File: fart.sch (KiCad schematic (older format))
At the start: 2 parts

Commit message: Add files via upload
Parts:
- U1: renamed from U?; footprint (none) -> Housings_DIP:DIP-40_W15.24mm_Socket_LongPads
- X1: renamed from X?; footprint (none) -> fart:Cart_Conn
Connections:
- net ROMC3: now reaches X1.10 (ROMC3)
- net ROMC3: now also U1.38 (ROMC3)
- net D3: now reaches X1.11 (D3)
- net D3: now also U1.19 (D3)
- net ROMC4: now reaches X1.12 (ROMC4)
- net ROMC4: now also U1.39 (ROMC4)
- net PHI: now reaches X1.13 (PHI)
- net PHI: now also U1.2 (PHI)
- net D4: now reaches X1.14 (D4)
- net D4: now also U1.21 (D4)
- net WRITE: now reaches X1.15 (WRITE)
- net WRITE: now also U1.3 (WRITE)
- net D5: now reaches X1.16 (D5)
- net D5: now also U1.22 (D5)
- net D6: now reaches X1.17 (D6)
- net D6: now also U1.23 (D6)
- net D7: now reaches X1.18 (D7)
- net D7: now also U1.24 (D7)
- net D0: now reaches X1.3 (D0)
- net D0: now also U1.16 (D0)
- net D1: now reaches X1.4 (D1)
- net D1: now also U1.17 (D1)
- net ~INTREQ: now reaches X1.5 (~INTREQ)
- net ~INTREQ: now also U1.4 (~INT_REQ)
- net ROMC0: now reaches X1.6 (ROMC0)
- net ROMC0: now also U1.35 (ROMC0)
- net ROMC1: now reaches X1.7 (ROMC1)
- net ROMC1: now also U1.36 (ROMC1)
- net ROMC2: now reaches X1.8 (ROMC2)
- net ROMC2: now also U1.37 (ROMC2)
- net D2: now reaches X1.9 (D2)
- net D2: now also U1.18 (D2)
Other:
- note added: "Vdd current: 70mA max"
- note added: "Vgg current: 70mA max"
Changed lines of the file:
@@
 $EndDescr
 $Comp
-L fart:CartConn X?
+L fart:CartConn X1
 U 1 1 5D1E5303
 P 7000 3100
-F 0 "X?" H 7228 3146 50  0000 L CNN
+F 0 "X1" H 7228 3146 50  0000 L CNN
 F 1 "CartConn" H 7228 3055 50  0000 L CNN
-F 2 "" H 6950 3100 50  0001 C CNN
+F 2 "fart:Cart_Conn" H 7000 1850 50  0000 C CNN
 F 3 "" H 6950 3100 50  0001 C CNN
 	1    7000 3100
@@
 $EndComp
 $Comp
-L fart:F3853 U?
+L fart:F3853 U1
 U 1 1 5D1E6D1B
 P 4000 3000
-F 0 "U?" H 4000 4175 50  0000 C CNN
+F 0 "U1" H 4000 4175 50  0000 C CNN
 F 1 "F3853" H 4000 4084 50  0000 C CNN
-F 2 "" H 4000 3000 50  0001 C CNN
+F 2 "Housings_DIP:DIP-40_W15.24mm_Socket_LongPads" H 4000 1900 50  0000 C CNN
 F 3 "" H 4000 3000 50  0001 C CNN
 	1    4000 3000
@@
 $EndComp
 $Comp
-L power:GND #PWR?
+L power:GND #PWR0101
 U 1 1 5D1E8B6D
 P 6400 2000
-F 0 "#PWR?" H 6400 1750 50  0001 C CNN
+F 0 "#PWR0101" H 6400 1750 50  0001 C CNN
 F 1 "GND" V 6405 1872 50  0001 R CNN
 F 2 "" H 6400 2000 50  0001 C CNN
@@
 	6500 2000 6400 2000
 $Comp
-L power:GND #PWR?
+L power:GND #PWR0102
 U 1 1 5D1E9405
 P 3400 3950
-F 0 "#PWR?" H 3400 3700 50  0001 C CNN
+F 0 "#PWR0102" H 3400 3700 50  0001 C CNN
 F 1 "GND" V 3405 3822 50  0001 R CNN
 F 2 "" H 3400 3950 50  0001 C CNN
@@
 $EndComp
 $Comp
-L power:+5V #PWR?
+L power:+5V #PWR0103
 U 1 1 5D1EA69B
 P 6450 3900
-F 0 "#PWR?" H 6450 3750 50  0001 C CNN
+F 0 "#PWR0103" H 6450 3750 50  0001 C CNN
 F 1 "+5V" V 6465 4028 50  0000 L CNN
 F 2 "" H 6450 3900 50  0001 C CNN
@@
 	6500 3900 6600 3900
 $Comp
-L power:+12V #PWR?
+L power:+12V #PWR0104
 U 1 1 5D1EBC41
 P 6600 4200
-F 0 "#PWR?" H 6600 4050 50  0001 C CNN
+F 0 "#PWR0104" H 6600 4050 50  0001 C CNN
 F 1 "+12V" V 6615 4328 50  0000 L CNN
 F 2 "" H 6600 4200 50  0001 C CNN
@@
 $EndComp
 $Comp
-L power:+5V #PWR?
+L power:+5V #PWR0105
 U 1 1 5D1EC708
 P 4600 2050
-F 0 "#PWR?" H 4600 1900 50  0001 C CNN
+F 0 "#PWR0105" H 4600 1900 50  0001 C CNN
 F 1 "+5V" V 4615 2178 50  0000 L CNN
 F 2 "" H 4600 2050 50  0001 C CNN
@@
 $EndComp
 $Comp
-L power:+12V #PWR?
+L power:+12V #PWR0106
 U 1 1 5D1ED13D
 P 3400 2050
-F 0 "#PWR?" H 3400 1900 50  0001 C CNN
+F 0 "#PWR0106" H 3400 1900 50  0001 C CNN
 F 1 "+12V" V 3415 2178 50  0000 L CNN
 F 2 "" H 3400 2050 50  0001 C CNN
@@
 	0    -1   -1   0
 $EndComp
+Text Notes 4750 1950 0    50   ~ 0
+Vdd current: 70mA max
+Text Notes 2300 1900 0    50   ~ 0
+Vgg current: 70mA max
+Text Label 6600 2500 2    50   ~ 0
+ROMC0
+Text Label 6600 2600 2    50   ~ 0
+ROMC1
+Text Label 6600 2700 2    50   ~ 0
+ROMC2
+Text Label 6600 2900 2    50   ~ 0
+ROMC3
+Text Label 6600 3200 2    50   ~ 0
+ROMC4
+Text Label 4600 2150 0    50   ~ 0
+ROMC4
+Text Label 4600 2250 0    50   ~ 0
+ROMC3
+Text Label 4600 2350 0    50   ~ 0
+ROMC2
+Text Label 4600 2450 0    50   ~ 0
+ROMC1
+Text Label 4600 2550 0    50   ~ 0
+ROMC0
+Text Label 6600 3300 2    50   ~ 0
+PHI
+Text Label 6600 3500 2    50   ~ 0
+WRITE
+Text Label 3400 2150 2    50   ~ 0
+PHI
+Text Label 3400 2250 2    50   ~ 0
+WRITE
+Text Label 6600 2400 2    50   ~ 0
+~INTREQ
+Text Label 3400 2350 2    50   ~ 0
+~INTREQ
+Text Label 3400 3550 2    50   ~ 0
+D0
+Text Label 3400 3650 2    50   ~ 0
+D1
+Text Label 3400 3750 2    50   ~ 0
+D2
+Text Label 3400 3850 2    50   ~ 0
+D3
+Text Label 4600 3950 0    50   ~ 0
+D4
+Text Label 4600 3850 0    50   ~ 0
+D5
+Text Label 4600 3750 0    50   ~ 0
+D6
+Text Label 4600 3650 0    50   ~ 0
+D7
+Text Label 6600 2200 2    50   ~ 0
+D0
+Text Label 6600 2300 2    50   ~ 0
+D1
+Text Label 6600 2800 2    50   ~ 0
+D2
+Text Label 6600 3000 2    50   ~ 0
+D3
+Text Label 6600 3400 2    50   ~ 0
+D4
+Text Label 6600 3600 2    50   ~ 0
+D5
+Text Label 6600 3700 2    50   ~ 0
+D6
+Text Label 6600 3800 2    50   ~ 0
+D7
 $EndSCHEMATC

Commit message: Add files via upload
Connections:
- net A5: now reaches U1.10 (A5)
- net A4: now reaches U1.11 (A4)
- net A3: now reaches U1.12 (A3)
- net A2: now reaches U1.13 (A2)
- net A1: now reaches U1.14 (A1)
- net A0: now reaches U1.15 (A0)
- net A8: now reaches U1.25 (A8)
- net A9: now reaches U1.26 (A9)
- net A10: now reaches U1.27 (A10)
- net A11: now reaches U1.28 (A11)
- net A12: now reaches U1.29 (A12)
- net A13: now reaches U1.30 (A13)
- net A14: now reaches U1.31 (A14)
- net A15: now reaches U1.32 (A15)
- net REGDR: now reaches U1.33 (REGDR)
- net CPU_READ: now reaches U1.34 (CPU_READ)
- net ~PRI_IN: now reaches U1.5 (~PRI_IN)
- net ~RAM_WRITE: now reaches U1.6 (~RAM_WRITE)
- net ~EXT_INT: now reaches U1.7 (~EXT_INT)
- net A7: now reaches U1.8 (A7)
- net A6: now reaches U1.9 (A6)
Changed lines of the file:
@@
 EESchema Schematic File Version 4
+LIBS:fart-cache
 EELAYER 29 0
 EELAYER END
@@
 Text Label 6600 3800 2    50   ~ 0
 D7
+Text Label 3400 3450 2    50   ~ 0
+A0
+Text Label 3400 3350 2    50   ~ 0
+A1
+Text Label 3400 3250 2    50   ~ 0
+A2
+Text Label 3400 3150 2    50   ~ 0
+A3
+Text Label 3400 3050 2    50   ~ 0
+A4
+Text Label 3400 2950 2    50   ~ 0
+A5
+Text Label 3400 2850 2    50   ~ 0
+A6
+Text Label 3400 2750 2    50   ~ 0
+A7
+Text Label 4600 3550 0    50   ~ 0
+A8
+Text Label 4600 3450 0    50   ~ 0
+A9
+Text Label 4600 3350 0    50   ~ 0
+A10
+Text Label 4600 3250 0    50   ~ 0
+A11
+Text Label 4600 3150 0    50   ~ 0
+A12
+Text Label 4600 3050 0    50   ~ 0
+A13
+Text Label 4600 2950 0    50   ~ 0
+A14
+Text Label 4600 2850 0    50   ~ 0
+A15
+Text Label 4600 2650 0    50   ~ 0
+CPU_READ
+Text Label 4600 2750 0    50   ~ 0
+REGDR
+Text Label 3400 2450 2    50   ~ 0
+~PRI_IN
+Text Label 3400 2550 2    50   ~ 0
+~RAM_WRITE
+Text Label 3400 2650 2    50   ~ 0
+~EXT_INT
 $EndSCHEMATC

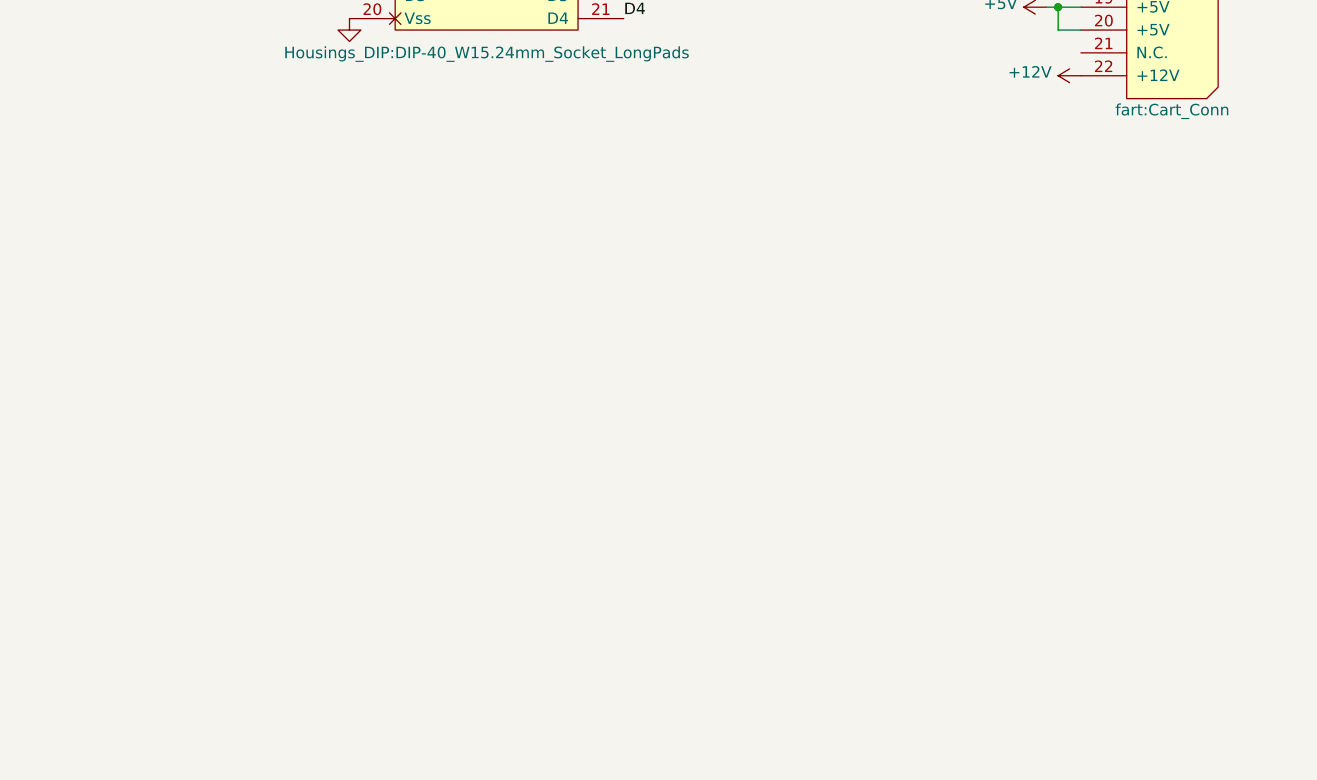
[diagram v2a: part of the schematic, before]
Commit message: Add EEPROM and address decoder
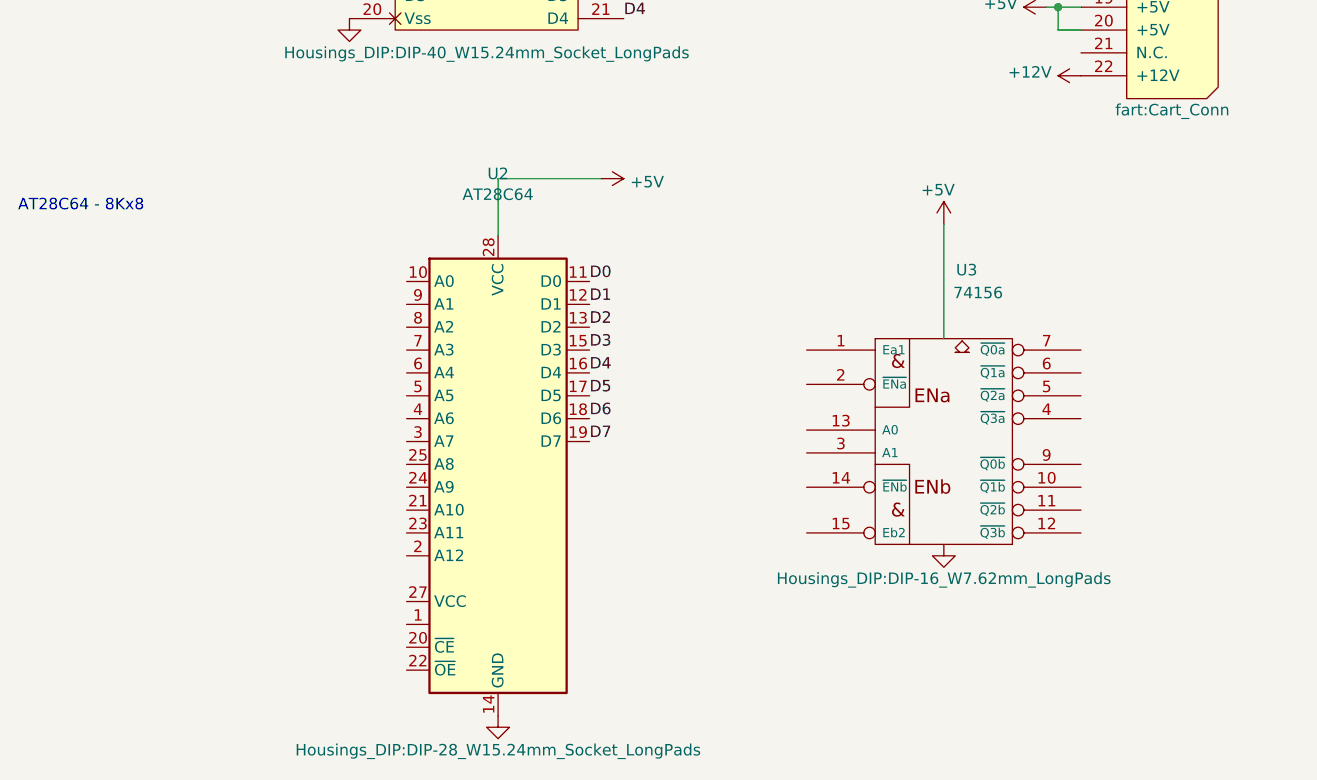
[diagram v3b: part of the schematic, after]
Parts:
- added U2: AT28C64, Housings_DIP:DIP-28_W15.24mm_Socket_LongPads, symbol fart:AT28C64
- added U3: 74156, Housings_DIP:DIP-16_W7.62mm_LongPads, symbol 74xx_IEEE:74156
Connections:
- net +5V: now also U2.28 (VCC), U3.16 (VCC)
- net D0: now also U2.11 (D0)
- net D1: now also U2.12 (D1)
- net D2: now also U2.13 (D2)
- net D3: now also U2.15 (D3)
- net D4: now also U2.16 (D4)
- net D5: now also U2.17 (D5)
- net D6: now also U2.18 (D6)
- net D7: now also U2.19 (D7)
- net GND: now also U2.14 (GND), U3.8 (GND)
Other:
- note added: "AT28C64 - 8Kx8"
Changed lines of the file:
@@
 Text Label 3400 2650 2    50   ~ 0
 ~EXT_INT
+$Comp
+L fart:AT28C64 U2
+U 1 1 5D1F340C
+P 4050 5900
+F 0 "U2" H 4050 7171 50  0000 C CNN
+F 1 "AT28C64" H 4050 7080 50  0000 C CNN
+F 2 "Housings_DIP:DIP-28_W15.24mm_Socket_LongPads" H 4050 4650 50  0000 C CNN
+F 3 "http://ww1.microchip.com/downloads/en/DeviceDoc/11107M.pdf" H 4050 5900 50  0001 C CNN
+	1    4050 5900
+	1    0    0    -1
+$EndComp
+$Comp
+L power:GND #PWR0107
+U 1 1 5D1F43A7
+P 4050 7000
+F 0 "#PWR0107" H 4050 6750 50  0001 C CNN
+F 1 "GND" V 4055 6872 50  0001 R CNN
+F 2 "" H 4050 7000 50  0001 C CNN
+F 3 "" H 4050 7000 50  0001 C CNN
+	1    4050 7000
+	1    0    0    -1
+$EndComp
+$Comp
+L power:+5V #PWR0108
+U 1 1 5D1F4C37
+P 4500 4650
+F 0 "#PWR0108" H 4500 4500 50  0001 C CNN
+F 1 "+5V" V 4515 4778 50  0000 L CNN
+F 2 "" H 4500 4650 50  0001 C CNN
+F 3 "" H 4500 4650 50  0001 C CNN
+	1    4500 4650
+	0    1    1    0
+$EndComp
+Wire Wire Line
+	4500 4650 4050 4650
+Wire Wire Line
+	4050 4650 4050 4900
+Text Notes 1950 4800 0    50   ~ 0
+AT28C64 - 8Kx8
+Text Label 4450 5100 0    50   ~ 0
+D0
+Text Label 4450 5200 0    50   ~ 0
+D1
+Text Label 4450 5300 0    50   ~ 0
+D2
+Text Label 4450 5400 0    50   ~ 0
+D3
+Text Label 4450 5500 0    50   ~ 0
+D4
+Text Label 4450 5600 0    50   ~ 0
+D5
+Text Label 4450 5700 0    50   ~ 0
+D6
+Text Label 4450 5800 0    50   ~ 0
+D7
+$Comp
+L 74xx_IEEE:74156 U3
+U 1 1 5D1FAB56
+P 6000 5800
+F 0 "U3" H 6100 6550 50  0000 C CNN
+F 1 "74156" H 6150 6450 50  0000 C CNN
+F 2 "Housings_DIP:DIP-16_W7.62mm_LongPads" H 6000 5200 50  0000 C CNN
+F 3 "" H 6000 5800 50  0001 C CNN
+	1    6000 5800
+	1    0    0    -1
+$EndComp
+$Comp
+L power:GND #PWR?
+U 1 1 5D1FD0AA
+P 6000 6250
+F 0 "#PWR?" H 6000 6000 50  0001 C CNN
+F 1 "GND" V 6005 6122 50  0001 R CNN
+F 2 "" H 6000 6250 50  0001 C CNN
+F 3 "" H 6000 6250 50  0001 C CNN
+	1    6000 6250
+	1    0    0    -1
+$EndComp
+$Comp
+L power:+5V #PWR?
+U 1 1 5D1FD8C8
+P 6000 4850
+F 0 "#PWR?" H 6000 4700 50  0001 C CNN
+F 1 "+5V" H 5900 5000 50  0000 L CNN
+F 2 "" H 6000 4850 50  0001 C CNN
+F 3 "" H 6000 4850 50  0001 C CNN
+	1    6000 4850
+	1    0    0    -1
+$EndComp
+Wire Wire Line
+	6000 4850 6000 5350
 $EndSCHEMATC

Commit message: Minor update
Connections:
- wire segments 11 -> 19
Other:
- note added: "0000 - BIOS\n0800 - CART\n1000 - \n1800 -\n2000 -\n2800 -\n3000 -\n3800 -"
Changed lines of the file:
@@
 Wire Wire Line
 	4050 4650 4050 4900
-Text Notes 1950 4800 0    50   ~ 0
+Text Notes 3050 4700 0    50   ~ 0
 AT28C64 - 8Kx8
 Text Label 4450 5100 0    50   ~ 0
@@
 Wire Wire Line
 	6000 4850 6000 5350
+Text Label 3650 5100 2    50   ~ 0
+A0
+Text Label 3650 5200 2    50   ~ 0
+A1
+Text Label 3650 5300 2    50   ~ 0
+A2
+Text Label 3650 5400 2    50   ~ 0
+A3
+Text Label 3650 5500 2    50   ~ 0
+A4
+Text Label 3650 5600 2    50   ~ 0
+A5
+Text Label 3650 5700 2    50   ~ 0
+A6
+Text Label 3650 5800 2    50   ~ 0
+A7
+Text Label 3650 5900 2    50   ~ 0
+A8
+Text Label 3650 6000 2    50   ~ 0
+A9
+Text Label 3650 6100 2    50   ~ 0
+A10
+$Comp
+L power:+5V #PWR?
+U 1 1 5D1F4388
+P 3650 6500
+F 0 "#PWR?" H 3650 6350 50  0001 C CNN
+F 1 "+5V" V 3665 6628 50  0000 L CNN
+F 2 "" H 3650 6500 50  0001 C CNN
+F 3 "" H 3650 6500 50  0001 C CNN
+	1    3650 6500
+	0    -1   -1   0
+$EndComp
+Text Label 5400 5750 2    50   ~ 0
+A11
+Text Label 5400 5850 2    50   ~ 0
+A12
+Text Notes 2000 5650 0    50   ~ 0
+0000 - BIOS\n0800 - CART\n1000 - \n1800 -\n2000 -\n2800 -\n3000 -\n3800 -
+Wire Wire Line
+	5400 6200 5100 6200
+Wire Wire Line
+	5100 6200 5100 5400
+Wire Wire Line
+	5100 5400 5400 5400
+Wire Wire Line
+	5400 5550 5200 5550
+Wire Wire Line
+	5200 5550 5200 6000
+Wire Wire Line
+	5200 6000 5400 6000
+Wire Wire Line
+	5100 5400 5000 5400
+Connection ~ 5100 5400
+Text Label 5000 5400 2    50   ~ 0
+A13
+Wire Wire Line
+	5200 6000 5000 6000
+Connection ~ 5200 6000
 $EndSCHEMATC

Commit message: Massive update
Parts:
- added U4: 74LS00, symbol 74xx:74LS00
- added U5: AT28C16, Housings_DIP:DIP-24_W15.24mm_Socket_LongPads, symbol fart:AT28C16
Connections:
- net labels added: 00xx, 08xx, 10xx, 18xx, 20xx, 28xx, 30xx, 38xx, ~CPU_READ
- wire segments 19 -> 37
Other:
- moved on the sheet: U2, U3

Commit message: Rough routing done
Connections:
- net CPU_READ: now also U4.12, U4.13; no longer U4.1, U4.2
- net ~CPU_READ: now also U4.11; no longer U4.3
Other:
- moved on the sheet: U4A, U4D
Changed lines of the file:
@@
 L 74xx:74LS00 U4
 U 1 1 5D22BA67
-P 5550 2650
-F 0 "U4" H 5550 2975 50  0000 C CNN
-F 1 "74LS00" H 5550 2884 50  0000 C CNN
-F 2 "" H 5550 2650 50  0001 C CNN
-F 3 "http://www.ti.com/lit/gpn/sn74ls00" H 5550 2650 50  0001 C CNN
-	1    5550 2650
+P 8700 4600
+F 0 "U4" H 8700 4925 50  0000 C CNN
+F 1 "74LS00" H 8700 4834 50  0000 C CNN
+F 2 "" H 8700 4600 50  0001 C CNN
+F 3 "http://www.ti.com/lit/gpn/sn74ls00" H 8700 4600 50  0001 C CNN
+	1    8700 4600
 	1    0    0    -1
 $EndComp
@@
 L 74xx:74LS00 U4
 U 4 1 5D231DC1
-P 9800 5750
-F 0 "U4" H 9800 6075 50  0000 C CNN
-F 1 "74LS00" H 9800 5984 50  0000 C CNN
-F 2 "" H 9800 5750 50  0001 C CNN
-F 3 "http://www.ti.com/lit/gpn/sn74ls00" H 9800 5750 50  0001 C CNN
-	4    9800 5750
+P 5550 2650
+F 0 "U4" H 5550 2975 50  0000 C CNN
+F 1 "74LS00" H 5550 2884 50  0000 C CNN
+F 2 "" H 5550 2650 50  0001 C CNN
+F 3 "http://www.ti.com/lit/gpn/sn74ls00" H 5550 2650 50  0001 C CNN
+	4    5550 2650
 	1    0    0    -1
 $EndComp

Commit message: Update
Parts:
- added C1: 47uF 16V, Capacitors_THT:CP_Radial_D5.0mm_P2.50mm, symbol Device:CP1
- added C5: 100nF, Capacitors_THT:C_Disc_D5.0mm_W2.5mm_P5.00mm, symbol Device:C
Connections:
- net +5V: now also C1.1, C5.1
- net GND: now also C1.2, C5.2
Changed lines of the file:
@@
 	1    0    0    -1
 $EndComp
+$Comp
+L Device:CP1 C1
+U 1 1 5D2DB74A
+P 8500 2750
+F 0 "C1" H 8615 2841 50  0000 L CNN
+F 1 "47uF 16V" H 8615 2750 50  0000 L CNN
+F 2 "Capacitors_THT:CP_Radial_D5.0mm_P2.50mm" H 8615 2659 50  0000 L CNN
+F 3 "~" H 8500 2750 50  0001 C CNN
+	1    8500 2750
+	1    0    0    -1
+$EndComp
+$Comp
+L power:+5V #PWR0115
+U 1 1 5D2DBF18
+P 8250 2500
+F 0 "#PWR0115" H 8250 2350 50  0001 C CNN
+F 1 "+5V" V 8265 2628 50  0000 L CNN
+F 2 "" H 8250 2500 50  0001 C CNN
+F 3 "" H 8250 2500 50  0001 C CNN
+	1    8250 2500
+	0    -1   -1   0
+$EndComp
+Wire Wire Line
+	8250 2500 8500 2500
+Wire Wire Line
+	8500 2500 8500 2600
+$Comp
+L power:GND #PWR0116
+U 1 1 5D2DDADE
+P 8500 2900
+F 0 "#PWR0116" H 8500 2650 50  0001 C CNN
+F 1 "GND" V 8505 2772 50  0001 R CNN
+F 2 "" H 8500 2900 50  0001 C CNN
+F 3 "" H 8500 2900 50  0001 C CNN
+	1    8500 2900
+	1    0    0    -1
+$EndComp
+$Comp
+L Device:C C5
+U 1 1 5D2DF90C
+P 10375 2700
+F 0 "C5" H 10490 2746 50  0000 L CNN
+F 1 "100nF" H 10490 2655 50  0000 L CNN
+F 2 "Capacitors_THT:C_Disc_D5.0mm_W2.5mm_P5.00mm" H 10413 2550 50  0001 C CNN
+F 3 "~" H 10375 2700 50  0001 C CNN
+	1    10375 2700
+	1    0    0    -1
+$EndComp
+$Comp
+L power:GND #PWR0117
+U 1 1 5D2DFB57
+P 10375 2900
+F 0 "#PWR0117" H 10375 2650 50  0001 C CNN
+F 1 "GND" V 10380 2772 50  0001 R CNN
+F 2 "" H 10375 2900 50  0001 C CNN
+F 3 "" H 10375 2900 50  0001 C CNN
+	1    10375 2900
+	1    0    0    -1
+$EndComp
+Wire Wire Line
+	10375 2900 10375 2850
+Wire Wire Line
+	8500 2500 10375 2500
+Wire Wire Line
+	10375 2500 10375 2550
+Connection ~ 8500 2500
 $EndSCHEMATC

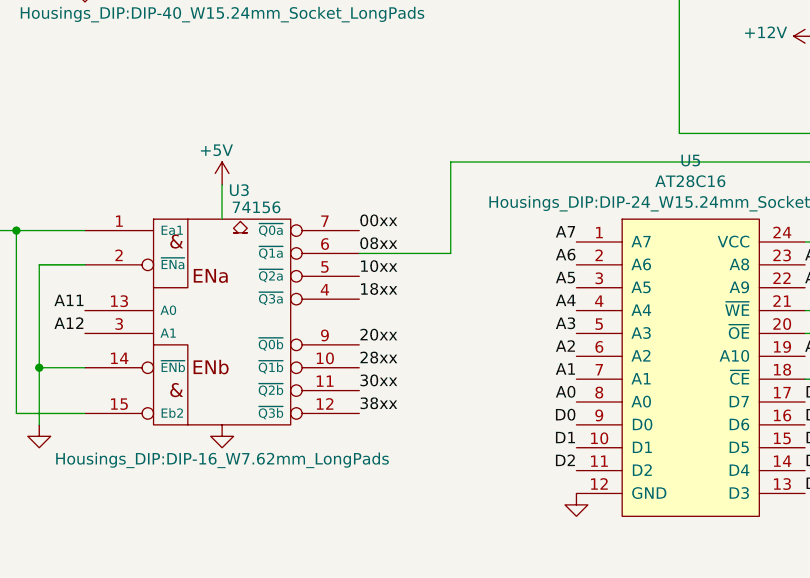
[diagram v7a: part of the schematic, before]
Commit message: Fixed wrong chip select (was on 2800h instead of 0800h)
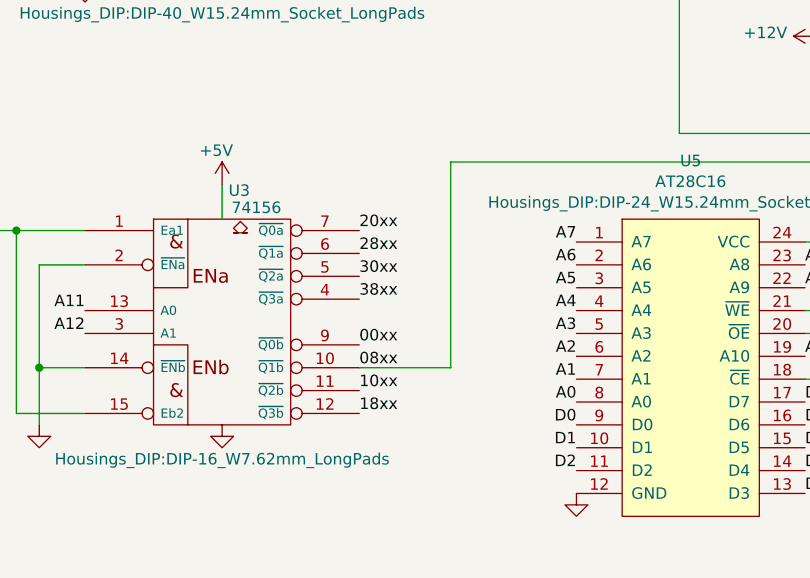
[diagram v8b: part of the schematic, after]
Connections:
- net 00xx: now also U3.9 (~Q0b); no longer U3.7 (~Q0a)
- net 08xx: now also U3.10 (~Q1b); no longer U3.6 (~Q1a)
- net 10xx: now also U3.11 (~Q2b); no longer U3.5 (~Q2a)
- net 18xx: now also U3.12 (~Q3b); no longer U3.4 (~Q3a)
- net 20xx: now also U3.7 (~Q0a); no longer U3.9 (~Q0b)
- net 28xx: now also U3.6 (~Q1a); no longer U3.10 (~Q1b)
- net 30xx: now also U3.5 (~Q2a); no longer U3.11 (~Q2b)
- net 38xx: now also U3.4 (~Q3a); no longer U3.12 (~Q3b)
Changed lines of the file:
@@
 	1    0    0    -1
 $EndComp
+Text Label 4600 5550 0    50   ~ 0
+00xx
+Text Label 4600 5650 0    50   ~ 0
+08xx
+Text Label 4600 5750 0    50   ~ 0
+10xx
+Text Label 4600 5850 0    50   ~ 0
+18xx
 Text Label 4600 5050 0    50   ~ 0
-00xx
+20xx
 Text Label 4600 5150 0    50   ~ 0
-08xx
+28xx
 Text Label 4600 5250 0    50   ~ 0
-10xx
+30xx
 Text Label 4600 5350 0    50   ~ 0
-18xx
-Text Label 4600 5550 0    50   ~ 0
-20xx
-Text Label 4600 5650 0    50   ~ 0
-28xx
-Text Label 4600 5750 0    50   ~ 0
-30xx
-Text Label 4600 5850 0    50   ~ 0
 38xx
 $Comp
@@
 A10
 Wire Wire Line
-	4600 5150 5000 5150
-Wire Wire Line
-	5000 5150 5000 4750
-Wire Wire Line
 	5000 4750 7250 4750
 Wire Wire Line
@@
 	10375 2500 10375 2550
 Connection ~ 8500 2500
+Wire Wire Line
+	5000 5650 4600 5650
+Wire Wire Line
+	5000 4750 5000 5650
 $EndSCHEMATC
